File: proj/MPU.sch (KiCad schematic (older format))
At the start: 51 parts, among them J6 JLINK, U12 ATSAM4S16CA-AU, U18 ATMEGA32U4-AU, X2 12MHz

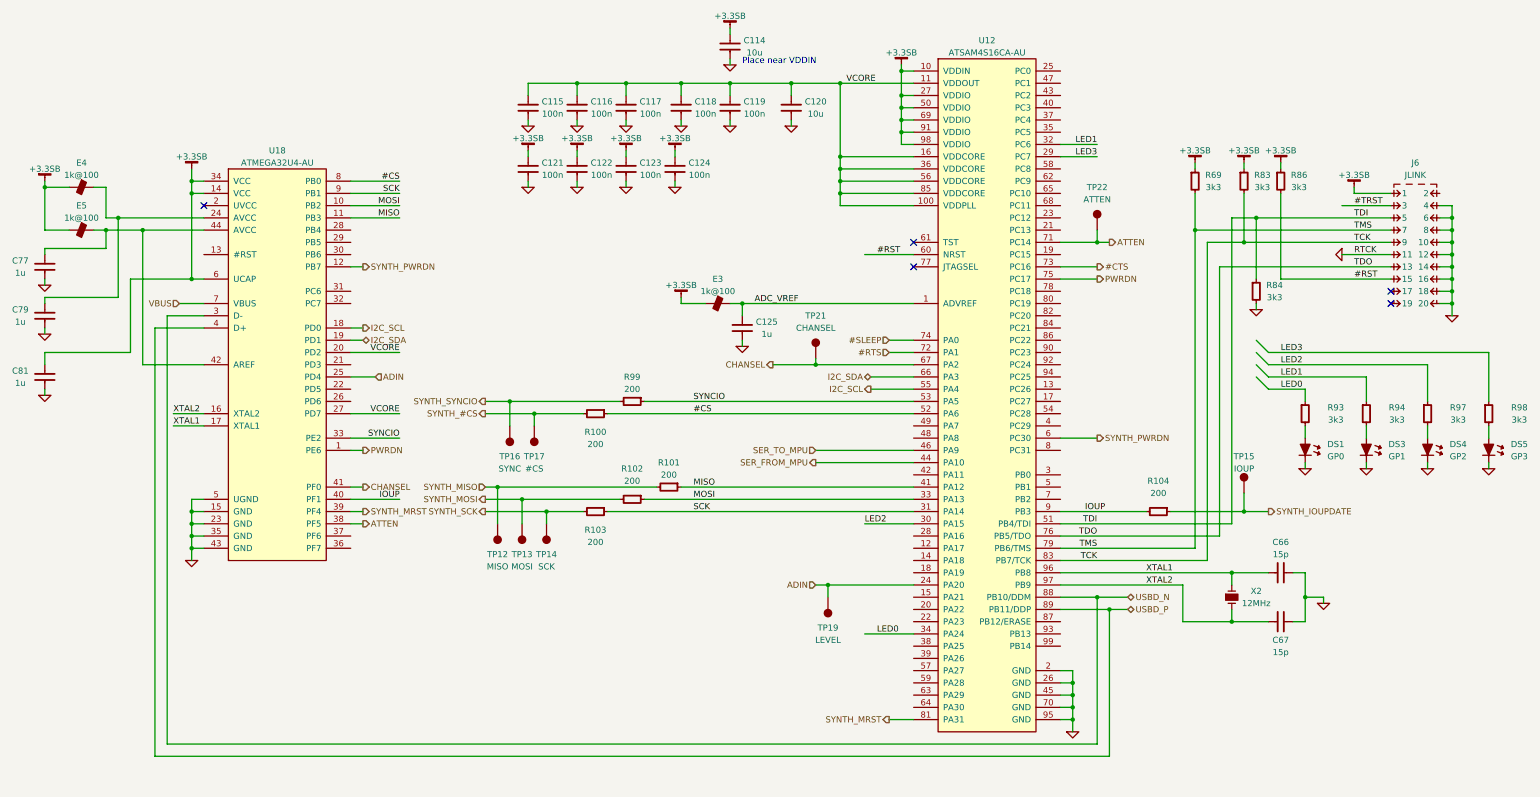
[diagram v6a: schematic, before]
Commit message: Connect ICSP for new MCU
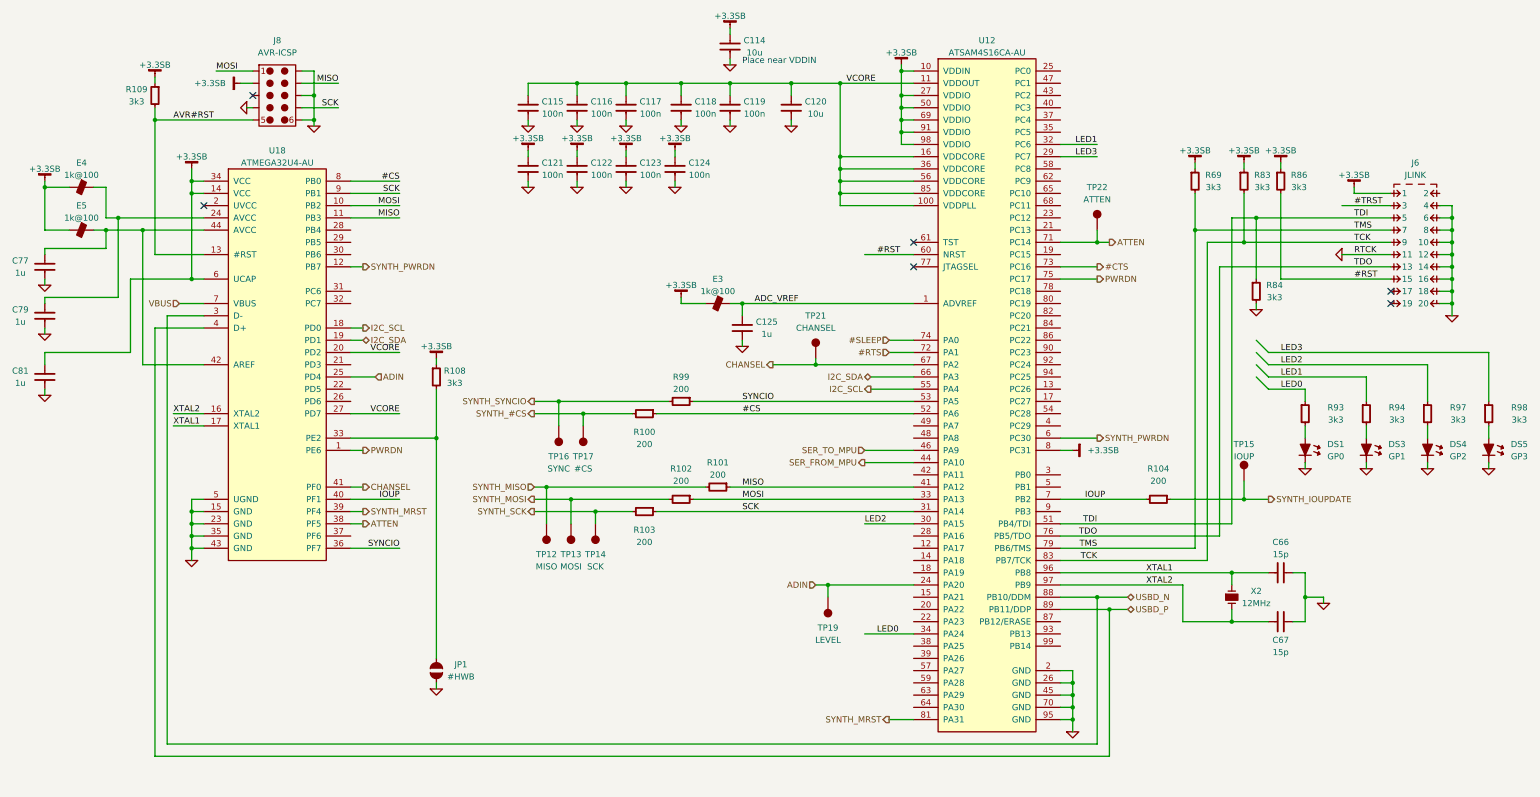
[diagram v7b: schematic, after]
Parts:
- added J8: AVR-ICSP, conn-test:TAGCONNECT-TC2050, symbol CONN-TAGCONNECT-TC2050
- added JP1: #HWB, symbol JUMPER-SOLDER
- added R108, R109: 3k3, IPC7351-Nominal:RESC1608X50, symbol R-0603
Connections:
- net +3.3SB: now also U12.8 (PC31), J8.2, R108.1, R109.1
- net GND: now also J8.10, J8.4, J8.6, J8.8, JP1.2
- net IOUP: now also U12.7 (PB2); no longer U12.9 (PB3)
- net MISO: now also J8.9
- net MOSI: now also J8.1
- net SCK: now also J8.7
- net SYNCIO: now also U18.36 (PF7); no longer U18.33 (PE2)
- net AVR#RST: now reaches U18.13 (#RST)
- net AVR#RST: now also J8.5, R109.2
- new net: JP1.1, R108.2, U18.33 (PE2)
- no-connect marks 5 -> 6
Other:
- moved on the sheet: R100, R101, R102, R103, R104, R99, TP12, TP13, TP14, TP15, TP16, TP17

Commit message: Tweaks
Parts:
- added C82: 100n-DNP, IPC7351-Nominal:CAPC1608X55, symbol C-0603
- C77, C79, C81: value 1u -> 1u-DNP; BOM CAP MLCC 1uF ≥X5R 10V 10% [0805] -> #CAP MLCC 1uF ≥X5R 10V 10% [0805]
- E4, E5: value 1k@100 -> 1k@100-DNP; BOM DIST DIGIKEY MZ1608-102YCT-ND -> #DIST DIGIKEY MZ1608-102YCT-ND
- R108, R109: value 3k3 -> 3k3-DNP; BOM RES SMD 3.3k 5% [0603] -> #RES SMD 3.3k 5% [0603]
- U18: value ATMEGA32U4-AU -> ATMEGA32U4-AU-DNP
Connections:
- net +3.3SB: now also C82.1
- net GND: now also C82.2
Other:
- moved on the sheet: C77, C79, C81, E5
